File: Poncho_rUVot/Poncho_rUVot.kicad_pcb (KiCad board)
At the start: 2 copper layers, 85.7 x 60.3 mm, 5 parts

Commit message: posicionamiento
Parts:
- removed G***: Logo_EDU-CIAA, footprint:Logo_EDU-CIAA
- removed G***: LOGO, footprint:Logo_Poncho
- removed G101: Logo_OSHWA, footprint:Logo_OSHWA
- removed MP?: Plantilla_EDU-CIAA, footprint:Plantilla_EDU-CIAA
- added BZ1: Buzzer, Buzzer_Beeper:Buzzer_12x9.5RM7.6, F.Cu at (96.0, 95.0)
- added D1: 1N4148, Diode_THT:D_DO-35_SOD27_P10.16mm_Horizontal, F.Cu at (91.0, 106.0)
- added D2: LED, LED_THT:LED_D5.0mm, F.Cu at (117.0, 118.0)
- added J1: Screw_Terminal_01x03, TerminalBlock_Phoenix:TerminalBlock_Phoenix_MKDS-1,5-3-5.08_1x03_P5.08mm_Horizontal, F.Cu at (98.0, 126.0)
- added K1: SANYOU_SRD_Form_C, Relay_THT:Relay_SPDT_SANYOU_SRD_Series_Form_C, F.Cu at (95.0, 111.0)
- added P1: Conn_01x03, Connector_PinHeader_2.54mm:PinHeader_1x03_P2.54mm_Horizontal, F.Cu at (135.5, 76.9)
- added P2: Conn_01x03, Connector_PinHeader_2.54mm:PinHeader_1x03_P2.54mm_Horizontal, F.Cu at (123.5, 76.9)
- added P3: Conn_01x04, Connector_PinHeader_2.54mm:PinHeader_1x04_P2.54mm_Horizontal, F.Cu at (109.5, 76.9)
- added P4: Conn_01x03, Connector_PinHeader_2.54mm:PinHeader_1x03_P2.54mm_Horizontal, F.Cu at (97.5, 76.9)
- added P5: Conn_01x02, Connector_PinHeader_2.54mm:PinHeader_1x02_P2.54mm_Horizontal, F.Cu at (78.4, 77.0)
- added P6: Conn_01x02, Connector_PinHeader_2.54mm:PinHeader_1x02_P2.54mm_Horizontal, F.Cu at (88.1, 76.9)
- added P7: Conn_01x06, Connector_PinSocket_2.54mm:PinSocket_1x06_P2.54mm_Vertical, F.Cu at (124.0, 115.0)
- added P8: Conn_01x04, Connector_PinHeader_2.54mm:PinHeader_1x04_P2.54mm_Horizontal, F.Cu at (64.0, 77.0)
- added P9: Conn_01x08, Connector_PinSocket_2.54mm:PinSocket_1x08_P2.54mm_Vertical, F.Cu at (124.0, 106.0)
- added Q1: BC548, Package_TO_SOT_THT:TO-92_Inline, F.Cu at (84.0, 120.0)
- added Q2: BC548, Package_TO_SOT_THT:TO-92_Inline, F.Cu at (82.0, 88.0)
- added R1: 220, Resistor_THT:R_Axial_DIN0204_L3.6mm_D1.6mm_P7.62mm_Horizontal, F.Cu at (83.0, 108.0)
- added R2: 220, Resistor_THT:R_Axial_DIN0204_L3.6mm_D1.6mm_P7.62mm_Horizontal, F.Cu at (83.0, 92.0)
- added R4: 470, Resistor_THT:R_Axial_DIN0204_L3.6mm_D1.6mm_P7.62mm_Horizontal, F.Cu at (117.0, 111.0)
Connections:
- XA101 pad 10: GNDA -> Net-(XA101-Pad10)
- XA101 pad 12: GNDA -> Net-(XA101-Pad12)
- XA101 pad 14: GNDA -> Net-(XA101-Pad14)
- XA101 pad 16: GNDA -> Net-(XA101-Pad16)
- XA101 pad 18: GNDA -> Net-(XA101-Pad18)
- XA101 pad 43: GNDD -> GND
- XA101 pad 45: GNDD -> GND
- XA101 pad 47: GNDD -> GND
- XA101 pad 51: GNDD -> GND
- XA101 pad 53: GNDD -> GND
- XA101 pad 57: GNDD -> GND
- XA101 pad 59: GNDD -> GND
- XA101 pad 65: GNDD -> GND
- XA101 pad 67: GNDD -> GND
- XA101 pad 7: GNDA -> Net-(XA101-Pad7)
- XA101 pad 77: GNDD -> GND
- XA101 pad 79: GNDD -> GND
- XA101 pad 8: GNDA -> Net-(XA101-Pad8)
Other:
- board size 85.7 x 60.3 mm -> 85.7 x 76 mm

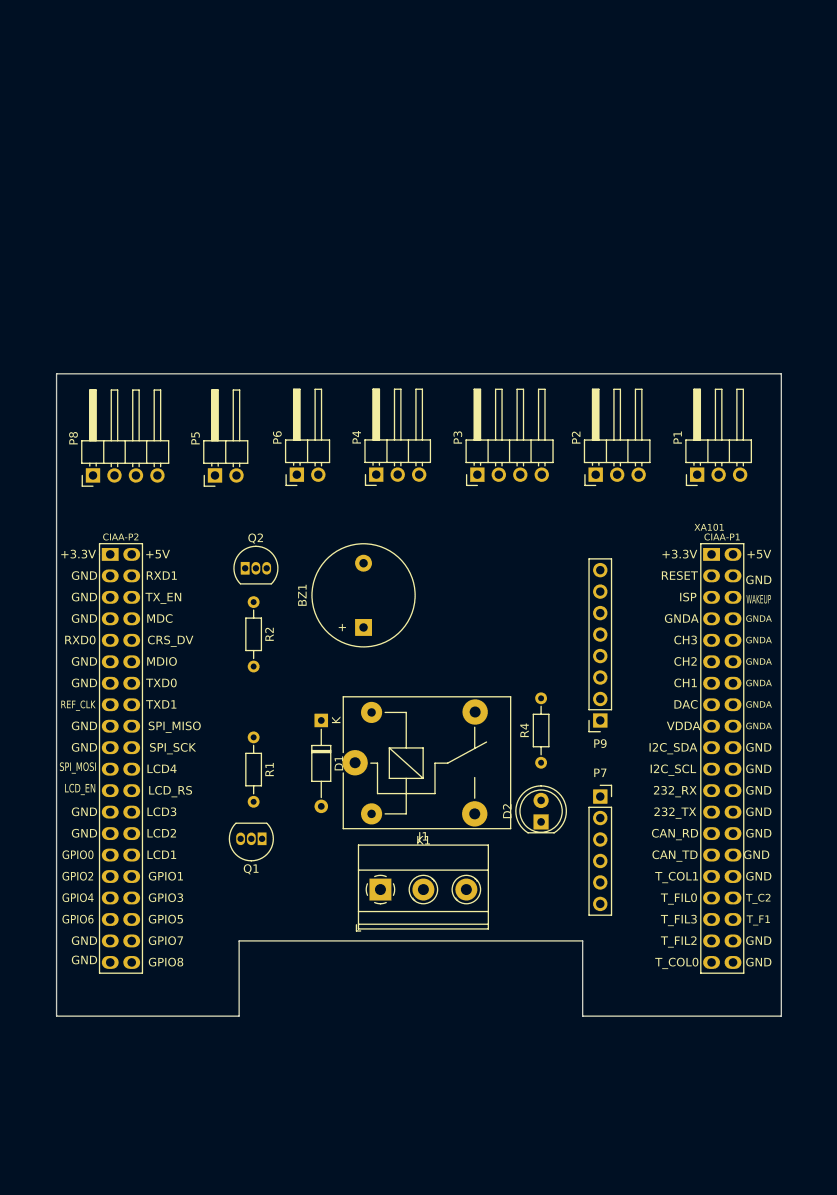
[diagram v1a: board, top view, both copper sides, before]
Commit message: Se agrega el PCB
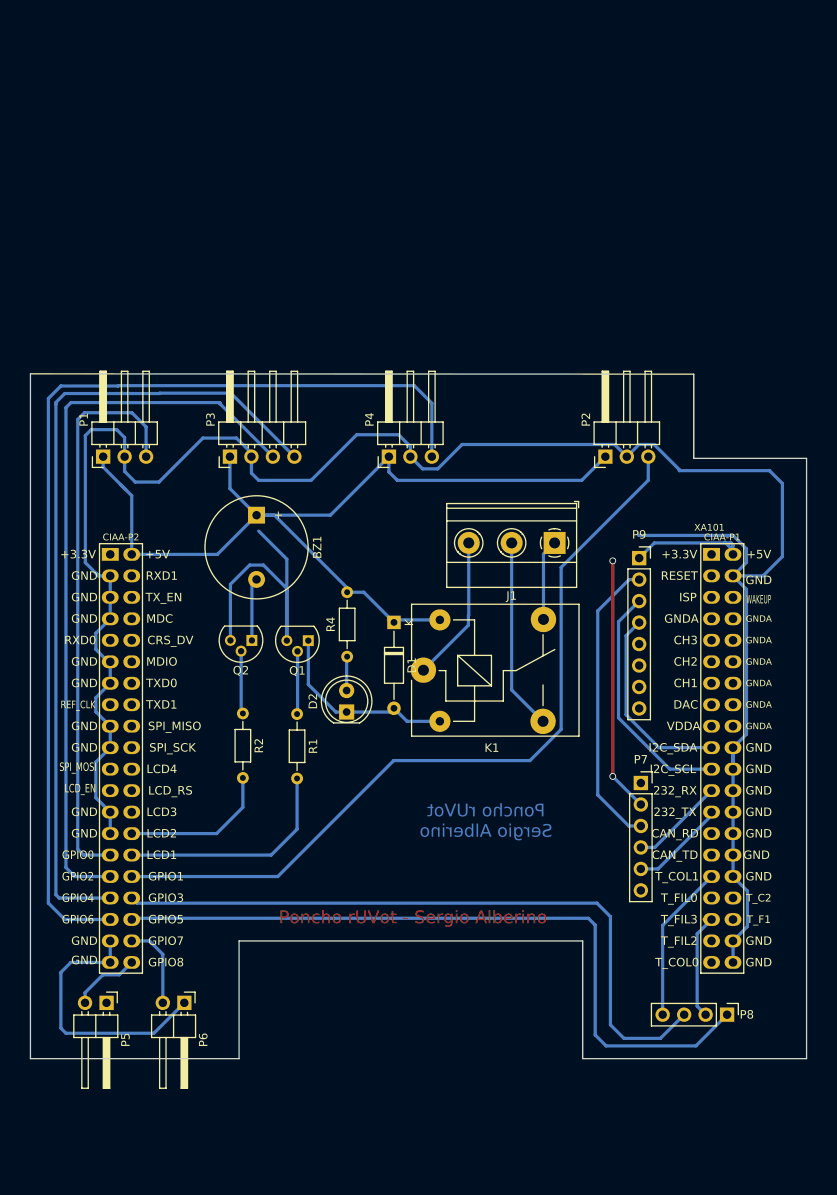
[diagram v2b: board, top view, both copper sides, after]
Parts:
- P8: footprint Connector_PinHeader_2.54mm:PinHeader_1x04_P2.54mm_Horizontal -> Connector_PinHeader_2.54mm:PinHeader_1x04_P2.54mm_Vertical
- Q1, Q2: footprint Package_TO_SOT_THT:TO-92_Inline -> Package_TO_SOT_THT:TO-92L
- moved P8 98.5 mm to (139.0, 140.8), turned to 270 degrees
- moved P1 70.3 mm to (65.2, 74.8)
- moved P6 63.9 mm to (74.8, 139.4), turned to 270 degrees
- moved P5 63.7 mm to (65.6, 139.4), turned to 270 degrees
- moved J1 45.9 mm to (118.6, 85.0), turned to 180 degrees
- moved P3 29.3 mm to (80.2, 74.8)
- moved D2 26.4 mm to (94.0, 105.0)
- moved R4 26.1 mm to (94.1, 98.5)
- moved Q1 24.1 mm to (89.5, 96.6)
- moved P9 19.7 mm to (128.6, 86.8), turned to 0 degrees
- moved BZ1 18.3 mm to (83.3, 81.7), turned to 270 degrees
- moved D1 14.4 mm to (99.6, 94.4)
- moved K1 13.6 mm to (103.1, 100.1)
- moved R2 13.2 mm to (81.7, 105.2)
- moved Q2 8.57 mm to (82.8, 96.5), turned to 180 degrees
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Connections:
- K1 pad 1: Net-(J1-Pad1) -> Net-(J1-Pad3)
- K1 pad 4: Net-(J1-Pad3) -> Net-(J1-Pad1)
- P4 pad 3: /GPIO8 -> /GPIO6
- P5 pad 2: /GPIO6 -> /GPIO8
- XA101 pad 42: +5VP -> +5V
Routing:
- net GND: track 0.00 -> 344.3 mm
- net +5V: track 0.00 -> 159.7 mm, vias 0 -> 2
- net /GPIO6: track 0.00 -> 121.0 mm
- net /GPIO4: track 0.00 -> 96.6 mm
- net /GPIO1: track 0.00 -> 94.5 mm
- net /GPIO2: track 0.00 -> 87.5 mm
- net /GPIO5: track 0.00 -> 85.9 mm
- net /GPIO3: track 0.00 -> 80.9 mm
- net /GPIO0: track 0.00 -> 67.6 mm
- net /SCL: track 0.00 -> 29.1 mm
- net /LCD1: track 0.00 -> 26.8 mm
- net /SDA: track 0.00 -> 23.5 mm
- net Net-(D1-Pad2): track 0.00 -> 23.0 mm
- net Net-(J1-Pad2): track 0.00 -> 22.6 mm
- net /T_COL1: track 0.00 -> 18.7 mm
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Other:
- board size 85.7 x 76 mm -> 91.8 x 81 mm
- net class Default: clearance 0.51 -> 0.3
- rule trace_clearance: 0.51 -> 0.3
- board text added: "Poncho rUVot - Sergio Alberino"
- board text added: "Poncho rUVot Sergio Alberino"
- board text added: "modulo Bluetooth"
- board text removed: "Borrar (Footprint MP1) la Plantilla-EDU-CIAA al finalizar el posicionamiento y definido el borde de PCB."
- board text removed: "Editar el rótulo"
- board text removed: "Editar este cuadro para reflejar cantidad de capas, si se han realizado cálculos de impedancia o si es relevante para el funcionamiento."
- board text removed: "PONCHO BASICO http://www.proyecto-ciaa.com.ar/"
- board text removed: "Se sugiere colocar Nombre de Poncho y autor en cobre, serigrafía y rótulo."

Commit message: Correcciones
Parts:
- moved J1 10.0 mm to (118.6, 75.0)
- moved P4 4.00 mm to (95.0, 74.8)
- moved P2 1.40 mm to (126.0, 74.8)
- moved P3 1.20 mm to (79.0, 74.8)
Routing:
- net GND: track 344.3 -> 380.1 mm, vias 0 -> 2
- net +5V: track 159.7 -> 131.1 mm
- net Net-(J1-Pad3): track 17.3 -> 27.8 mm
- net Net-(J1-Pad2): track 22.6 -> 33.2 mm
- net Net-(J1-Pad1): track 9.60 -> 19.6 mm
- net /GPIO6: track 121.0 -> 116.3 mm
- net /GPIO1: track 94.5 -> 98.9 mm
- net /GPIO2: track 87.5 -> 86.3 mm
- net /GPIO4: track 96.6 -> 95.4 mm
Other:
- board text added: "C NC NA"

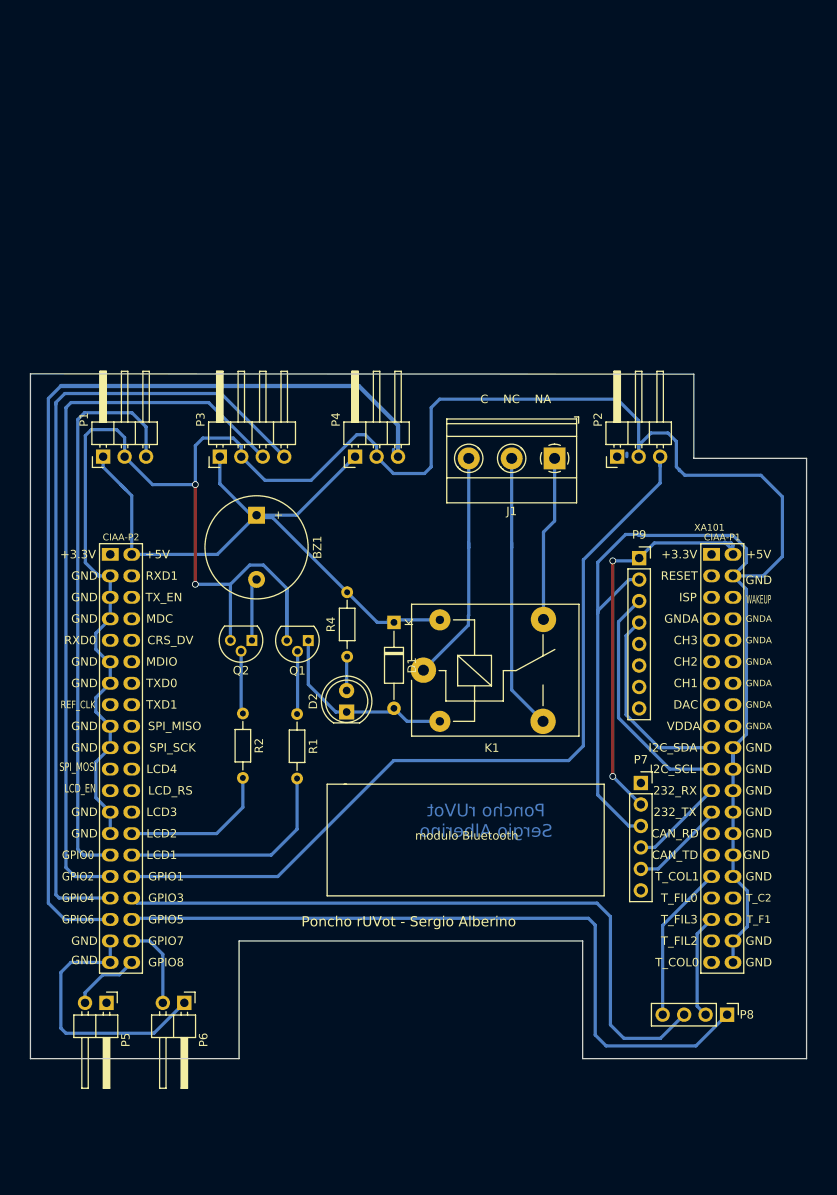
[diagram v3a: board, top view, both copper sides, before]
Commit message: Correcciones de tamaño de pista
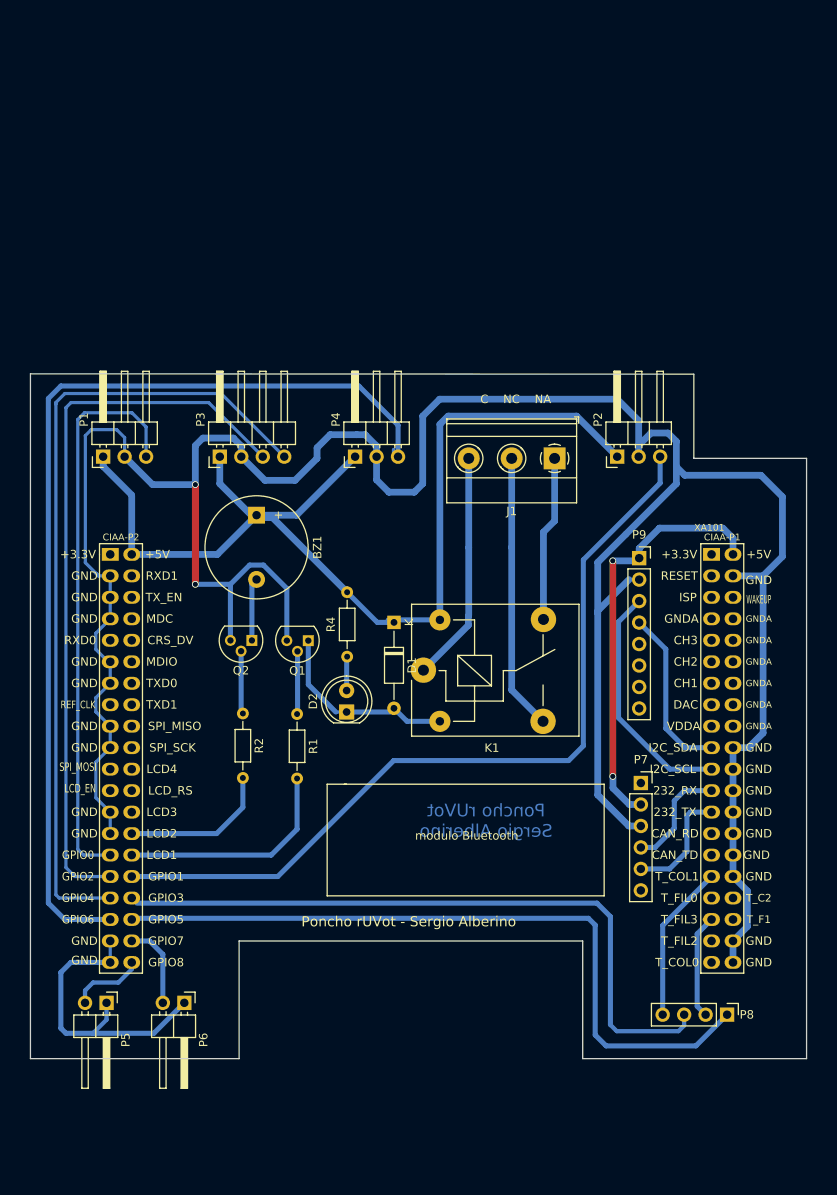
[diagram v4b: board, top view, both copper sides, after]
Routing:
- net +5V: track 131.1 -> 179.1 mm
- net /RS232_TXD: track 11.6 -> 15.0 mm
- net /SDA: track 23.5 -> 20.4 mm
- net /RS232_RXD: track 11.3 -> 13.3 mm
- net GND: track 380.1 -> 381.1 mm
- net /GPIO8: track 8.20 -> 8.82 mm

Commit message: Correcciones
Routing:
- net GND: track 381.1 -> 380.4 mm
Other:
- board text added: "Diseño simple faz. Sin requerimientos especiales. pistas: 0,6 mm y 0,8mm Margen: Distancia al borde: Documentaciòn superficial: HASL"
- board text removed: "Diseño simple faz. Sin requerimientos especiales."
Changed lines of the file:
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@@
     (thickness 1.6)
     (drawings 42)
-    (tracks 280)
+    (tracks 277)
     (zones 0)
     (modules 20)
@@
     (mod_text_size 0.15 0.15)
     (mod_text_width 0.02)
-    (pad_size 1.4 1.4)
-    (pad_drill 0.6)
+    (pad_size 2.6 2.6)
+    (pad_drill 1.3)
     (pad_to_mask_clearance 0.2)
     (aux_axis_origin 0 0)
@@
   (gr_line (start 148.4 146) (end 121.92 146) (angle 90) (layer Edge.Cuts) (width 0.15))
   (gr_line (start 148.4 75) (end 148.4 146) (angle 90) (layer Edge.Cuts) (width 0.15))
-  (gr_text "Diseño simple faz.\nSin requerimientos especiales." (at 194.945 24.13) (layer Dwgs.User)
-    (effects (font (size 1.5 1.5) (thickness 0.3)) (justify left))
+  (gr_text "Diseño simple faz.\nSin requerimientos especiales.\npistas: 0,6 mm y 0,8mm \nMargen: \nDistancia al borde: \nDocumentaciòn superficial: HASL\n" (at 191.75 33.25) (layer Dwgs.User)
+    (effects (font (size 1.8 1.8) (thickness 0.4)) (justify left))
   )
   (gr_text STACK-UP (at 227.965 19.05) (layer Dwgs.User)
-    (effects (font (size 1.5 1.5) (thickness 0.3)))
+    (effects (font (size 1.8 1.8) (thickness 0.4)))
   )
   (gr_line (start 278.765 16.51) (end 186.69 16.51) (angle 90) (layer Dwgs.User) (width 0.2))
@@
   (segment (start 66.04 109.22) (end 64.33949 110.92051) (width 0.381) (layer B.Cu) (net 2))
   (segment (start 66.04 116.84) (end 66.04 119.38) (width 0.381) (layer B.Cu) (net 2))
-  (segment (start 67.74 72.54) (end 67.74 74.8) (width 0.381) (layer B.Cu) (net 2))
-  (segment (start 64.659 88.9) (end 63.09101 87.33201) (width 0.381) (layer B.Cu) (net 2))
-  (segment (start 63.09101 87.33201) (end 63.09101 72.30899) (width 0.381) (layer B.Cu) (net 2))
-  (segment (start 66.04 88.9) (end 64.659 88.9) (width 0.381) (layer B.Cu) (net 2))
-  (segment (start 63.09101 72.30899) (end 63.8 71.6) (width 0.381) (layer B.Cu) (net 2))
-  (segment (start 63.8 71.6) (end 66.8 71.6) (width 0.381) (layer B.Cu) (net 2))
-  (segment (start 66.8 71.6) (end 67.74 72.54) (width 0.381) (layer B.Cu) (net 2))
-  (segment (start 64.659 88.9) (end 64.339499 88.580499) (width 0.381) (layer B.Cu) (net 2))
+  (segment (start 67.74 72.54) (end 67.74 74.8) (width 0.8) (layer B.Cu) (net 2))
+  (segment (start 63.8 71.6) (end 66.8 71.6) (width 0.8) (layer B.Cu) (net 2))
+  (segment (start 66.8 71.6) (end 67.74 72.54) (width 0.8) (layer B.Cu) (net 2))
   (segment (start 86.92684 90.387038) (end 86.92684 90.67316) (width 0.381) (layer B.Cu) (net 2))
   (segment (start 80.25384 89.896398) (end 80.25384 96.5327) (width 0.6) (layer B.Cu) (net 2))
@@
   (segment (start 92.05 72.2) (end 95.2 72.2) (width 0.8) (layer B.Cu) (net 2))
   (segment (start 90.5 73.75) (end 92.05 72.2) (width 0.8) (layer B.Cu) (net 2))
+  (segment (start 66.04 88.9) (end 64.9 88.9) (width 0.8) (layer B.Cu) (net 2))
+  (segment (start 64.9 88.9) (end 63.25 87.25) (width 0.8) (layer B.Cu) (net 2))
+  (segment (start 63.25 72.15) (end 63.8 71.6) (width 0.8) (layer B.Cu) (net 2))
+  (segment (start 63.25 87.25) (end 63.25 72.15) (width 0.8) (layer B.Cu) (net 2))
   (segment (start 136.922 109.22) (end 137.16 109.22) (width 1) (layer F.Cu) (net 9))
   (segment (start 137.16 109.22) (end 134.03 109.22) (width 0.6) (layer B.Cu) (net 9))
@@
   (segment (start 78.62 119.38) (end 68.58 119.38) (width 0.6) (layer B.Cu) (net 41))
   (segment (start 81.72704 116.27296) (end 78.62 119.38) (width 0.6) (layer B.Cu) (net 41))
-  (segment (start 66.04 121.92) (end 62.88 121.92) (width 0.381) (layer B.Cu) (net 42))
-  (segment (start 62.88 121.92) (end 62.2 121.24) (width 0.381) (layer B.Cu) (net 42))
-  (segment (start 62.2 121.24) (end 62.2 70.4) (width 0.381) (layer B.Cu) (net 42))
-  (segment (start 62.2 70.4) (end 63 69.6) (width 0.381) (layer B.Cu) (net 42))
-  (segment (start 63 69.6) (end 68.6 69.6) (width 0.381) (layer B.Cu) (net 42))
-  (segment (start 70.28 71.28) (end 70.28 74.8) (width 0.381) (layer B.Cu) (net 42))
-  (segment (start 68.6 69.6) (end 70.28 71.28) (width 0.381) (layer B.Cu) (net 42))
+  (segment (start 66.04 121.92) (end 62.88 121.92) (width 0.6) (layer B.Cu) (net 42))
+  (segment (start 62.88 121.92) (end 62.2 121.24) (width 0.6) (layer B.Cu) (net 42))
+  (segment (start 62.2 121.24) (end 62.2 70.4) (width 0.6) (layer B.Cu) (net 42))
+  (segment (start 62.2 70.4) (end 63 69.6) (width 0.6) (layer B.Cu) (net 42))
+  (segment (start 63 69.6) (end 68.6 69.6) (width 0.6) (layer B.Cu) (net 42))
+  (segment (start 70.28 71.28) (end 70.28 74.8) (width 0.6) (layer B.Cu) (net 42))
+  (segment (start 68.6 69.6) (end 70.28 71.28) (width 0.6) (layer B.Cu) (net 42))
   (segment (start 88.13546 112.86236) (end 88.13546 118.86454) (width 0.6) (layer B.Cu) (net 43))
   (segment (start 85.08 121.92) (end 68.58 121.92) (width 0.6) (layer B.Cu) (net 43))
   (segment (start 88.13546 118.86454) (end 85.08 121.92) (width 0.6) (layer B.Cu) (net 43))
-  (segment (start 66.04 124.46) (end 61.86 124.46) (width 0.381) (layer B.Cu) (net 44))
-  (segment (start 61.86 124.46) (end 60.8 123.4) (width 0.381) (layer B.Cu) (net 44))
-  (segment (start 60.8 69) (end 61.4 68.4) (width 0.381) (layer B.Cu) (net 44))
-  (segment (start 60.8 123.4) (end 60.8 69) (width 0.381) (layer B.Cu) (net 44))
-  (segment (start 77.68 68.4) (end 84.08 74.8) (width 0.381) (layer B.Cu) (net 44))
-  (segment (start 61.4 68.4) (end 77.68 68.4) (width 0.381) (layer B.Cu) (net 44))
+  (segment (start 84.08 74.57198) (end 84.08 74.8) (width 0.508) (layer B.Cu) (net 44))
+  (segment (start 66.04 124.46) (end 61.96 124.46) (width 0.508) (layer B.Cu) (net 44))
+  (segment (start 60.46502 122.96502) (end 60.46502 70.53498) (width 0.508) (layer B.Cu) (net 44))
+  (segment (start 61.96 124.46) (end 60.46502 122.96502) (width 0.508) (layer B.Cu) (net 44))
+  (segment (start 60.46502 70.53498) (end 62.5 68.5) (width 0.508) (layer B.Cu) (net 44))
+  (segment (start 84.08 74.730828) (end 84.08 74.8) (width 0.508) (layer B.Cu) (net 44))
+  (segment (start 77.849172 68.5) (end 84.08 74.730828) (width 0.508) (layer B.Cu) (net 44))
+  (segment (start 62.5 68.5) (end 77.849172 68.5) (width 0.508) (layer B.Cu) (net 44))
   (segment (start 131.08 75.92) (end 131.08 74.8) (width 0.381) (layer B.Cu) (net 45))
   (segment (start 131.08 77.92) (end 131.08 74.8) (width 0.6) (layer B.Cu) (net 45))
@@
   (segment (start 122 109) (end 122 87) (width 0.6) (layer B.Cu) (net 45))
   (segment (start 122 87) (end 131.08 77.92) (width 0.6) (layer B.Cu) (net 45))
-  (segment (start 66.04 127) (end 60.8 127) (width 0.381) (layer B.Cu) (net 46))
-  (segment (start 60 127) (end 59.61101 126.61101) (width 0.381) (layer B.Cu) (net 46))
-  (segment (start 60.8 127) (end 60 127) (width 0.381) (layer B.Cu) (net 46))
-  (segment (start 59.61101 126.61101) (end 59.61101 68.6) (width 0.381) (layer B.Cu) (net 46))
-  (segment (start 59.61101 68.38899) (end 60.66899 67.33101) (width 0.381) (layer B.Cu) (net 46))
-  (segment (start 59.61101 68.6) (end 59.61101 68.38899) (width 0.381) (layer B.Cu) (net 46))
-  (segment (start 67.46899 67.33101) (end 67.50899 67.29101) (width 0.381) (layer B.Cu) (net 46))
-  (segment (start 60.66899 67.33101) (end 67.46899 67.33101) (width 0.381) (layer B.Cu) (net 46))
-  (segment (start 79.15101 67.33101) (end 86.62 74.8) (width 0.381) (layer B.Cu) (net 46))
-  (segment (start 67.46899 67.33101) (end 79.15101 67.33101) (width 0.381) (layer B.Cu) (net 46))
+  (segment (start 79.11401 67.29401) (end 86.62 74.8) (width 0.508) (layer B.Cu) (net 46))
+  (segment (start 60.553742 67.29401) (end 79.11401 67.29401) (width 0.508) (layer B.Cu) (net 46))
+  (segment (start 59.57401 126.57401) (end 59.57401 68.273742) (width 0.508) (layer B.Cu) (net 46))
+  (segment (start 59.57401 68.273742) (end 60.553742 67.29401) (width 0.508) (layer B.Cu) (net 46))
+  (segment (start 66.04 127) (end 60 127) (width 0.508) (layer B.Cu) (net 46))
+  (segment (start 60 127) (end 59.57401 126.57401) (width 0.508) (layer B.Cu) (net 46))
   (segment (start 69.185791 127.605791) (end 68.58 127) (width 0.381) (layer B.Cu) (net 47))
   (segment (start 125.2 129.2) (end 123.605791 127.605791) (width 0.6) (layer B.Cu) (net 47))
